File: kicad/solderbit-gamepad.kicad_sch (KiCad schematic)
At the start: 28 parts, among them J1 Microbit, SW1 MST22D18G2 125, U1 74HC165

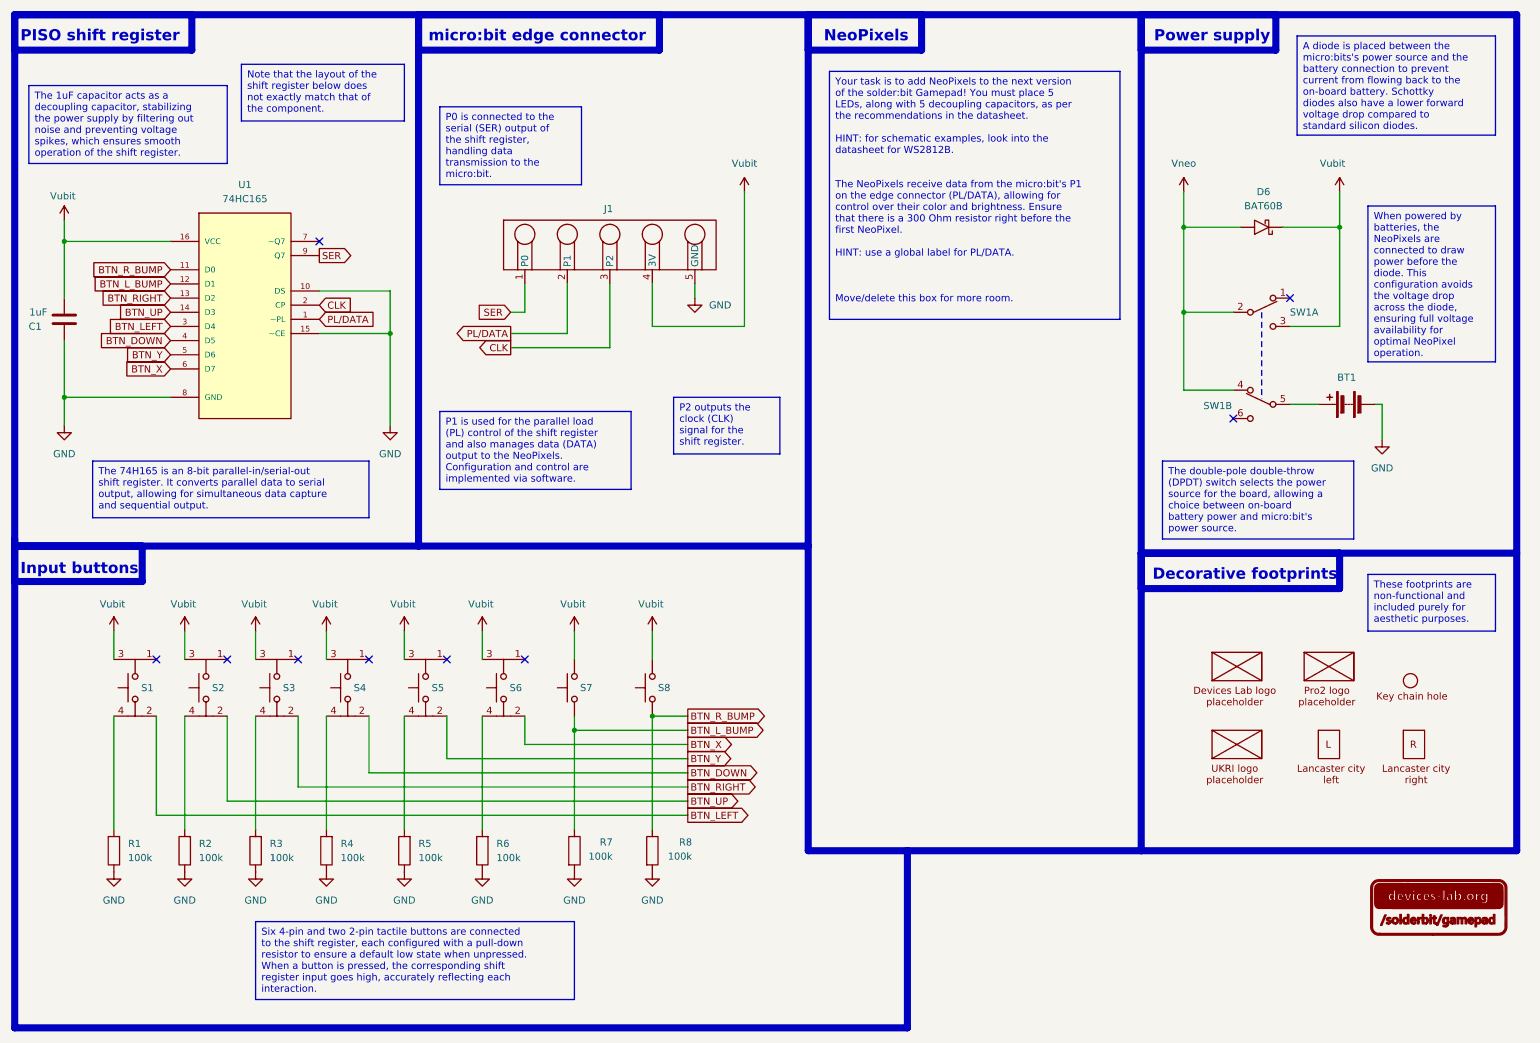
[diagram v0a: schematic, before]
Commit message: Added all new project files and updated README.md for 2025 workshop
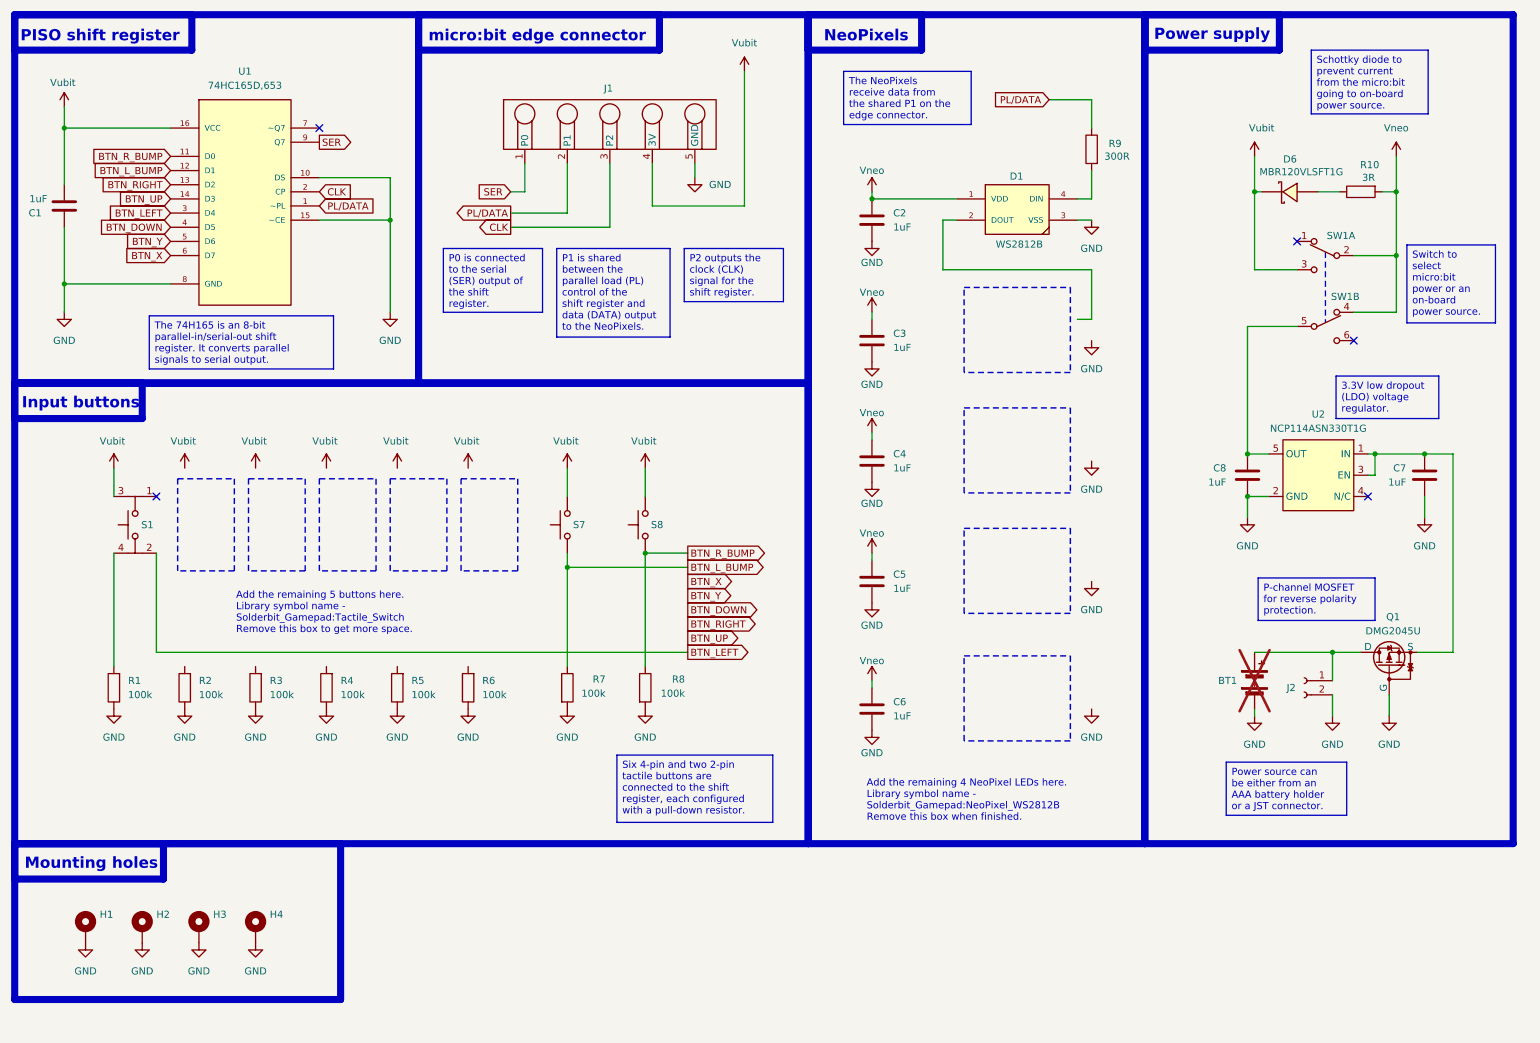
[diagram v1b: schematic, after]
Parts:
- removed D6: BAT60B, Solderbit_Gamepad:Schottky_Diode_SOD-323, symbol Solderbit_Gamepad:Schottky_Diode
- removed G1: ~, Solderbit_Gamepad:Devices-Lab_Logo_H9mm, symbol Solderbit_Gamepad:Devices-Lab_Logo_Placeholder
- removed G2: ~, Solderbit_Gamepad:Pro2_Logo, symbol Solderbit_Gamepad:Pro2_Logo_Placeholder
- removed G3: ~, Solderbit_Gamepad:Key_Chain_Hole, symbol Solderbit_Gamepad:Key_Chain_Hole
- removed G4: ~, Solderbit_Gamepad:UKRI_Logo, symbol Solderbit_Gamepad:UKRI_Logo_Placeholder
- removed G5: ~, Solderbit_Gamepad:LSS_L, symbol Solderbit_Gamepad:LSS_Left
- removed G6: ~, Solderbit_Gamepad:LSS_R, symbol Solderbit_Gamepad:LSS_Right
- removed S2, S3, S4, S5, S6: TS-1002S-AR06026, Solderbit_Gamepad:Tactile_Switch, symbol Solderbit_Gamepad:Tactile_Switch_4_Pin
- added C2, C3, C4, C5, C6, C7, C8: 1uF, Solderbit_Gamepad:1206_Capacitor, symbol Solderbit_Gamepad:Capacitor
- added D1: WS2812B, Solderbit_Gamepad:NeoPixel_WS2812B, symbol Solderbit_Gamepad:NeoPixel_WS2812B
- added D6: MBR120VLSFT1G, Solderbit_Gamepad:SOD-123FL, symbol Solderbit_Gamepad:MBR120VLSFT1G
- added H1, H2, H3, H4: MountingHole_Pad, Solderbit_Gamepad:MountingHole_Pad, symbol Mechanical:MountingHole_Pad
- added J2: S2B-PH-SM4-TB(LF)(SN), Solderbit_Gamepad:JST_PH_S2B-PH-SM4-TB, symbol Connector:Conn_01x02_Socket
- added Q1: DMG2045U, Solderbit_Gamepad:TSOT-23, symbol Solderbit_Gamepad:DMG2045U
- added R10: 3R, Solderbit_Gamepad:1206_Resistor, symbol Solderbit_Gamepad:Resistor
- added R9: 300R, Solderbit_Gamepad:1206_Resistor, symbol Solderbit_Gamepad:Resistor
- added U2: NCP114ASN330T1G, Solderbit_Gamepad:TSOP-5, symbol Solderbit_Gamepad:NCP114ASN330T1G
- BT1: Basic (none) -> No; LCSC Part (none) -> C964881; Package (none) -> SMD; now not fitted
- C1: Basic (none) -> Yes; LCSC Part (none) -> C1848; Package (none) -> 1206
- J1: value Microbit -> Microbit_Edge_Connector
- R1, R2, R3, R4, R5, R6, R7, R8: Basic (none) -> Yes; LCSC Part (none) -> C17900; Package (none) -> 1206
- S1: value TS-1002S-AR06026 -> KH-6X6X6H-STM; Basic (none) -> No; LCSC Part (none) -> C2837532; Package (none) -> SMD
- S7, S8: Basic (none) -> No; LCSC Part (none) -> C499324; Package (none) -> SMD,6x6mm
- SW1: Basic (none) -> No; LCSC Part (none) -> C2906280; Package (none) -> SMD
- U1: value 74HC165 -> 74HC165D,653; Basic (none) -> No; LCSC Part (none) -> C5613; Package (none) -> SOIC-16
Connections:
- net GND: now also C2.2, C3.2, C4.2, C5.2, C6.2, C7.2, C8.2, D1.3 (VSS), H1.1, H2.1, H3.1, H4.1, J2.2 (Pin_2), Q1.1 (G), U2.2 (GND)
- net PL/DATA: now also R9.2
- net Vneo: now also C2.1, C3.1, C4.1, C5.1, C6.1, D1.1 (VDD), R10.1
- net Vubit: now also D6.1
- net at SW1.5 (B): now also C8.1, U2.5 (OUT); no longer BT1.1 (+)
- new net: C7.1, Q1.2 (S), U2.1 (IN), U2.3 (EN)
- new net: BT1.1 (+), J2.1 (Pin_1), Q1.3 (D)
- new net: D1.4 (DIN), R9.1
- new net: D6.2, R10.2
- no-connect marks 9 -> 5
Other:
- note added: "Mounting holes"
- note removed: "Decorative footprints"
- company: pro² network+ -> pro² network+ summer school 2025
- moved on the sheet: C1, J1, R1, R2, R3, R4, R5, R6, R7, R8, S1, S7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
